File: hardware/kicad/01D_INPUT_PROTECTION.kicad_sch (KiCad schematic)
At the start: 0 parts

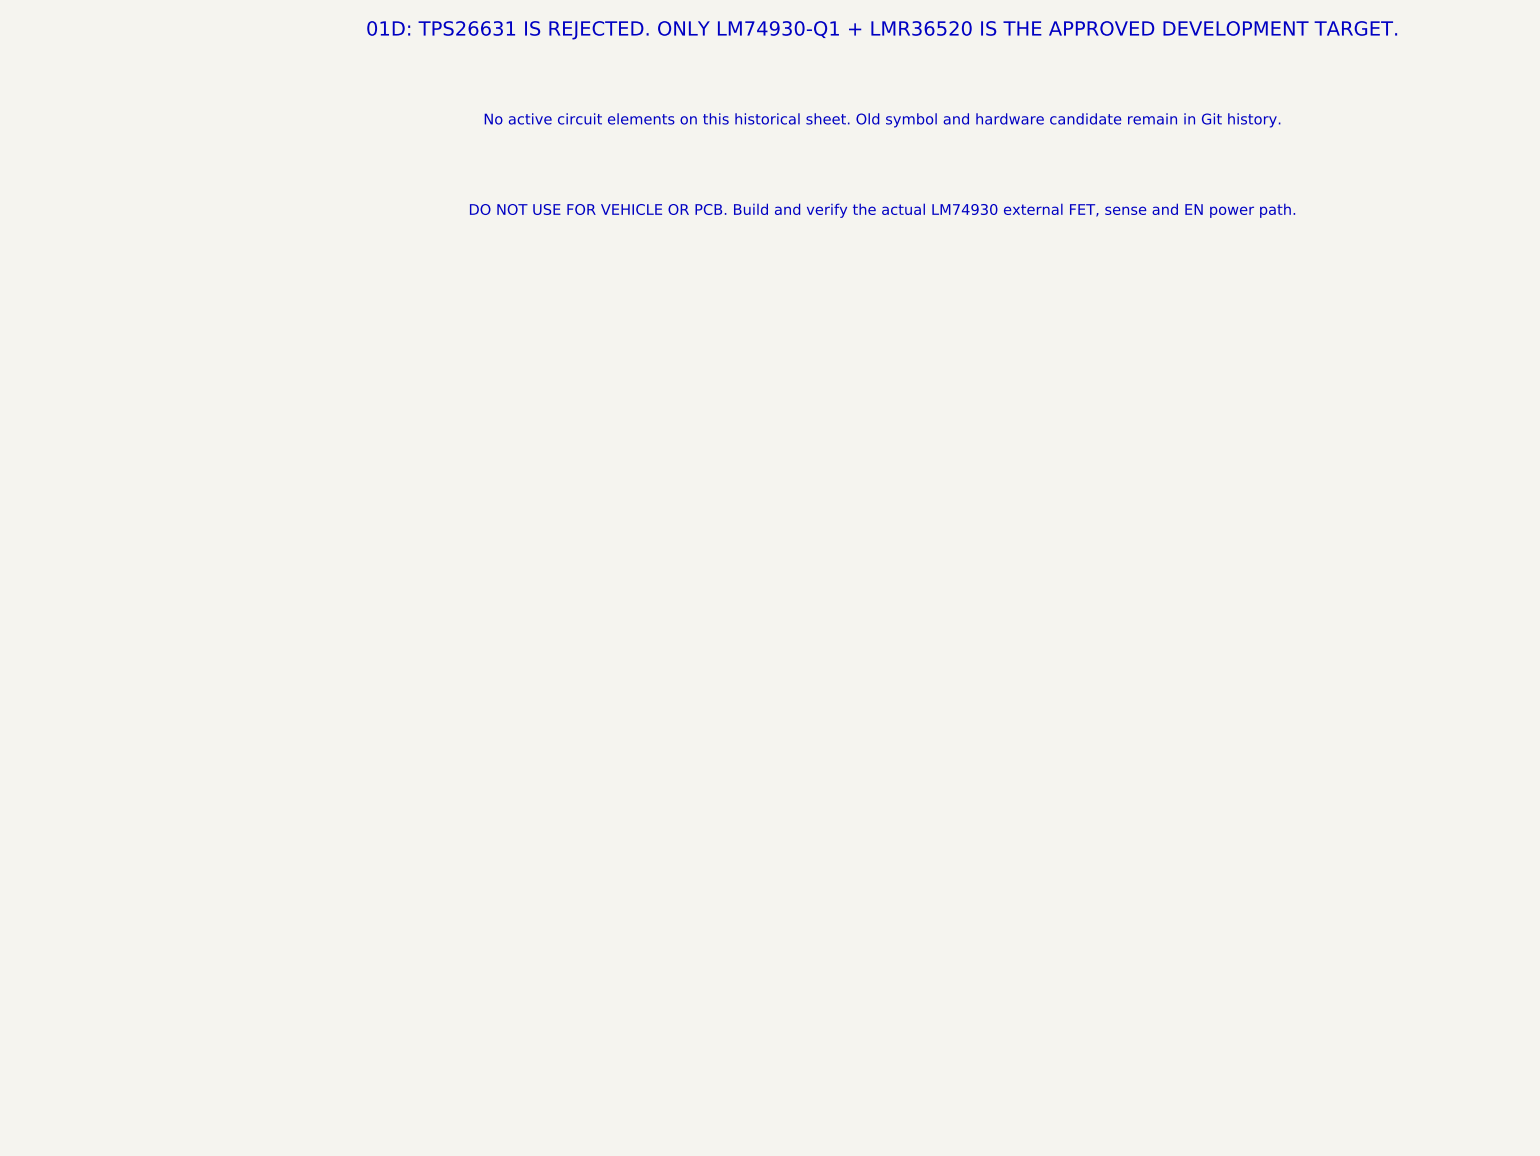
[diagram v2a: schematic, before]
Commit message: hardware(kicad): place LM74930-Q1 controller and datasheet-required 100nF capacitors in active 01D
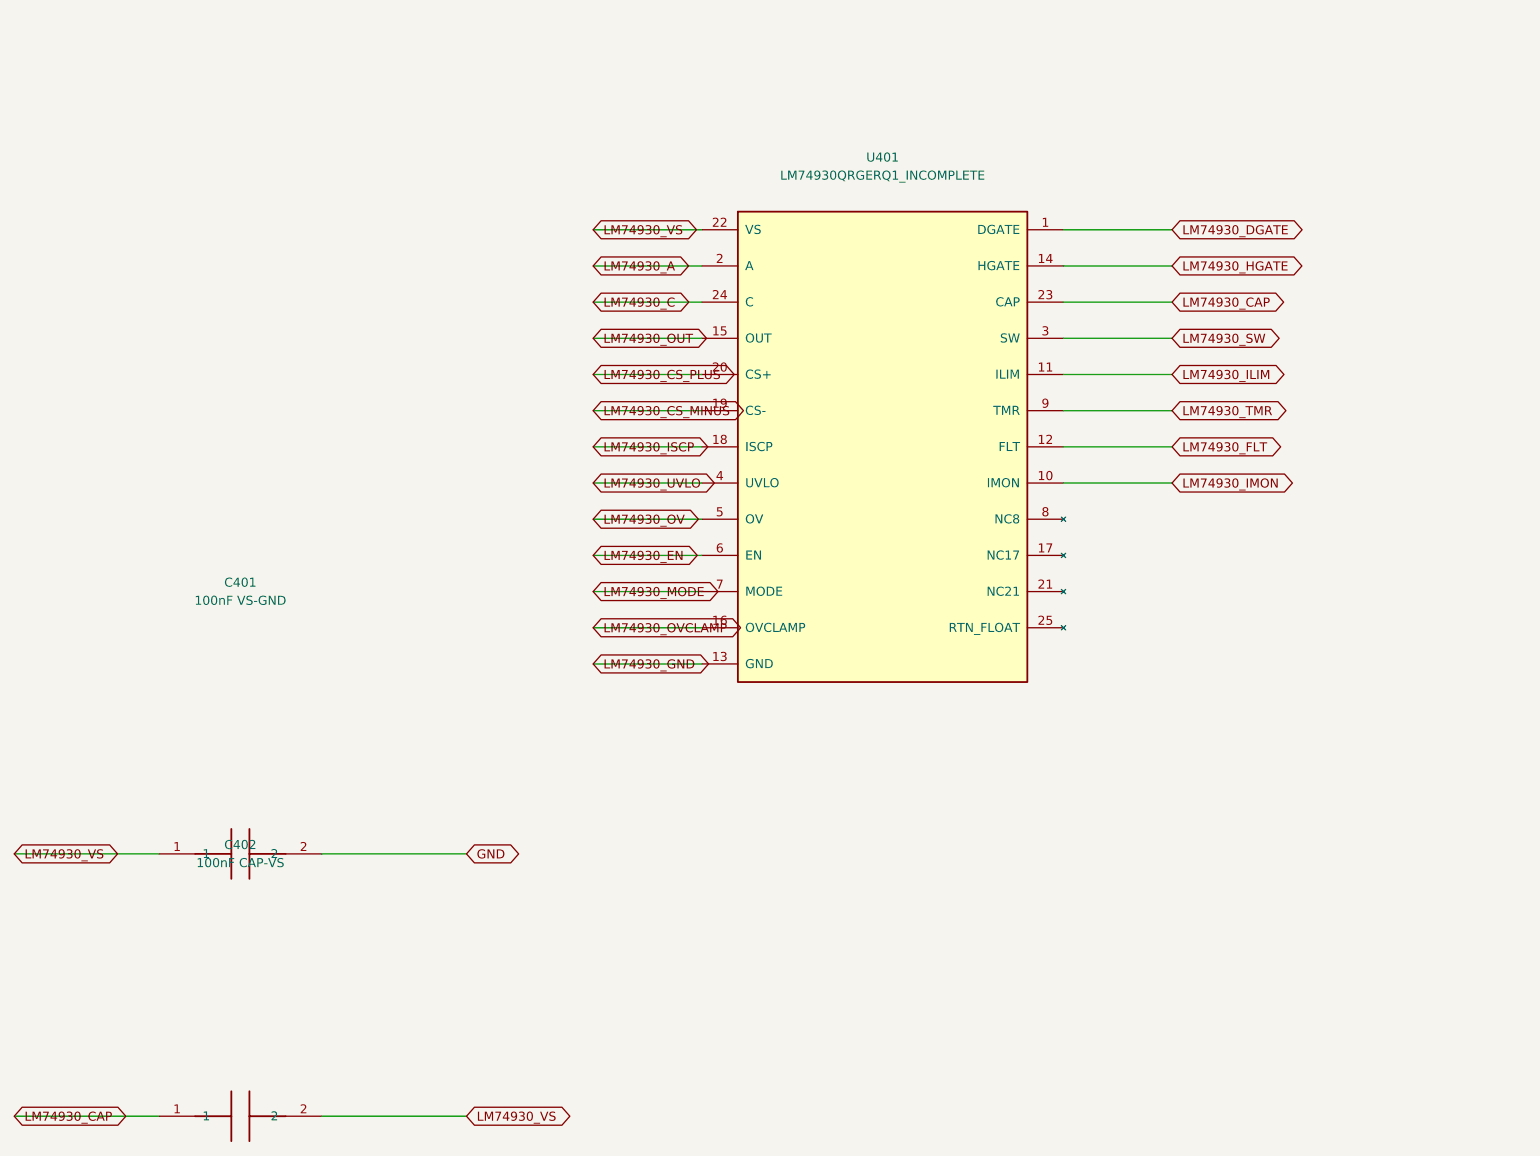
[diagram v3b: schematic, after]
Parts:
- added C401: 100nF VS-GND, Tripmaster:C_1206_3216, symbol Tripmaster_Sym:C
- added C402: 100nF CAP-VS, Tripmaster:C_1206_3216, symbol Tripmaster_Sym:C
- added U401: LM74930QRGERQ1_INCOMPLETE, Tripmaster:TI_LM74930_RGE0024T_FLOAT_EP, symbol TripTracer_V1:LM74930_Q1_RGE
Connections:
- new net GND: C401.2
- new net LM74930_A: U401.2 (A)
- new net LM74930_C: U401.24 (C)
- new net LM74930_CAP: C402.1, U401.23 (CAP)
- new net LM74930_CS_MINUS: U401.19 (CS-)
- new net LM74930_CS_PLUS: U401.20 (CS+)
- new net LM74930_DGATE: U401.1 (DGATE)
- new net LM74930_EN: U401.6 (EN)
- new net LM74930_FLT: U401.12 (FLT)
- new net LM74930_GND: U401.13 (GND)
- new net LM74930_HGATE: U401.14 (HGATE)
- new net LM74930_ILIM: U401.11 (ILIM)
- new net LM74930_IMON: U401.10 (IMON)
- new net LM74930_ISCP: U401.18 (ISCP)
- new net LM74930_MODE: U401.7 (MODE)
- new net LM74930_OUT: U401.15 (OUT)
- new net LM74930_OV: U401.5 (OV)
- new net LM74930_OVCLAMP: U401.16 (OVCLAMP)
- new net LM74930_SW: U401.3 (SW)
- new net LM74930_TMR: U401.9 (TMR)
- new net LM74930_UVLO: U401.4 (UVLO)
- new net LM74930_VS: C401.1, C402.2, U401.22 (VS)
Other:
- note removed: "01D: TPS26631 IS REJECTED. ONLY LM74930-Q1 + LMR36520 IS THE APPROVED DEVELOPMENT TARGET."
- note removed: "DO NOT USE FOR VEHICLE OR PCB. Build and verify the actual LM74930 external FET, sense and EN power path."
- note removed: "No active circuit elements on this historical sheet. Old symbol and hardware candidate remain in Git history."
- title: TripTracer V1 - 01D retired TPS26631 candidate -> TripTracer V1 - 01D LM74930-Q1 controller integration
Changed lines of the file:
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@@
-(kicad_sch (version 20250114) (generator "eeschema")
- (paper "A3")
- (title_block (title "TripTracer V1 - 01D retired TPS26631 candidate") (date "2026-10-14") (rev "RETired / LM74930-Q1 ONLY / NOT WIRED"))
- (text "01D: TPS26631 IS REJECTED. ONLY LM74930-Q1 + LMR36520 IS THE APPROVED DEVELOPMENT TARGET." (at 190.5 76.2 0) (effects (font (size 2 2))))
- (text "No active circuit elements on this historical sheet. Old symbol and hardware candidate remain in Git history." (at 190.5 88.9 0) (effects (font (size 1.5 1.5))))
- (text "DO NOT USE FOR VEHICLE OR PCB. Build and verify the actual LM74930 external FET, sense and EN power path." (at 190.5 101.6 0) (effects (font (size 1.5 1.5))))
- (sheet_instances (path "/a26d9b0c-7f10-4e5a-a65f-000000000064/a26d9b0c-7f10-4e5a-a65f-000000000065" (page "2.4")))
- (embedded_fonts no)
-)

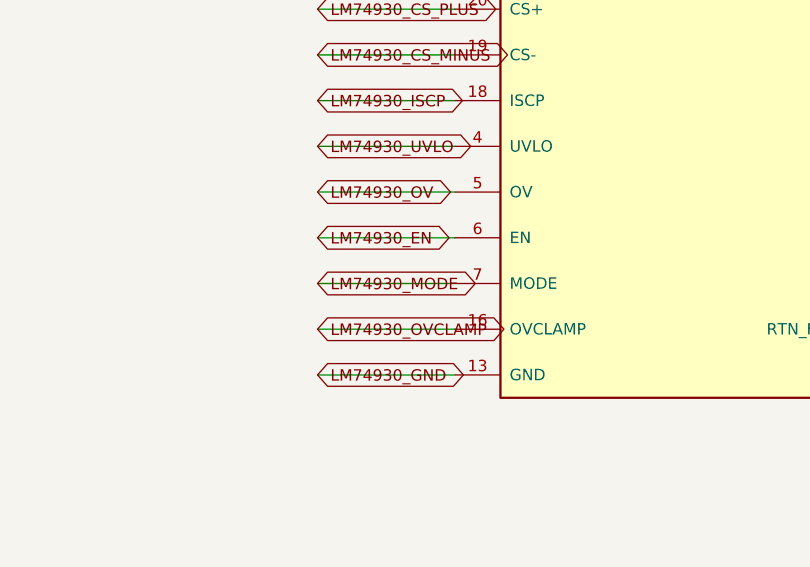
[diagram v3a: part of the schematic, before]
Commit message: hardware(power): tie LM74930 MODE high to VS to preserve reverse-current blocking
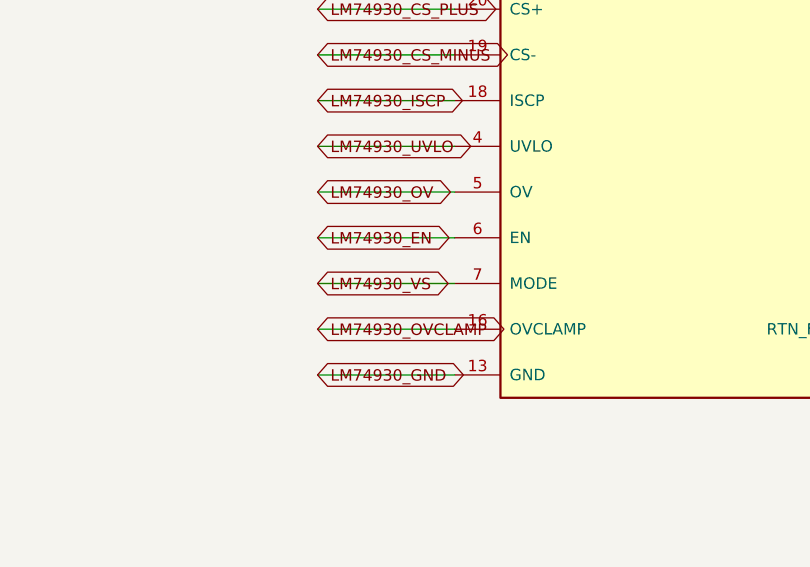
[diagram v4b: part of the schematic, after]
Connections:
- net LM74930_MODE is gone; now on net LM74930_VS: U401.7 (MODE)

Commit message: hardware(power): correct LM74930 VS capacitor to 1uF min nominal 1210 per load-dump design guidance
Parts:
- C401: value 100nF VS-GND -> 1uF >=100V VS-GND (Ceff verify); footprint Tripmaster:C_1206_3216 -> Tripmaster:C_1210_3225

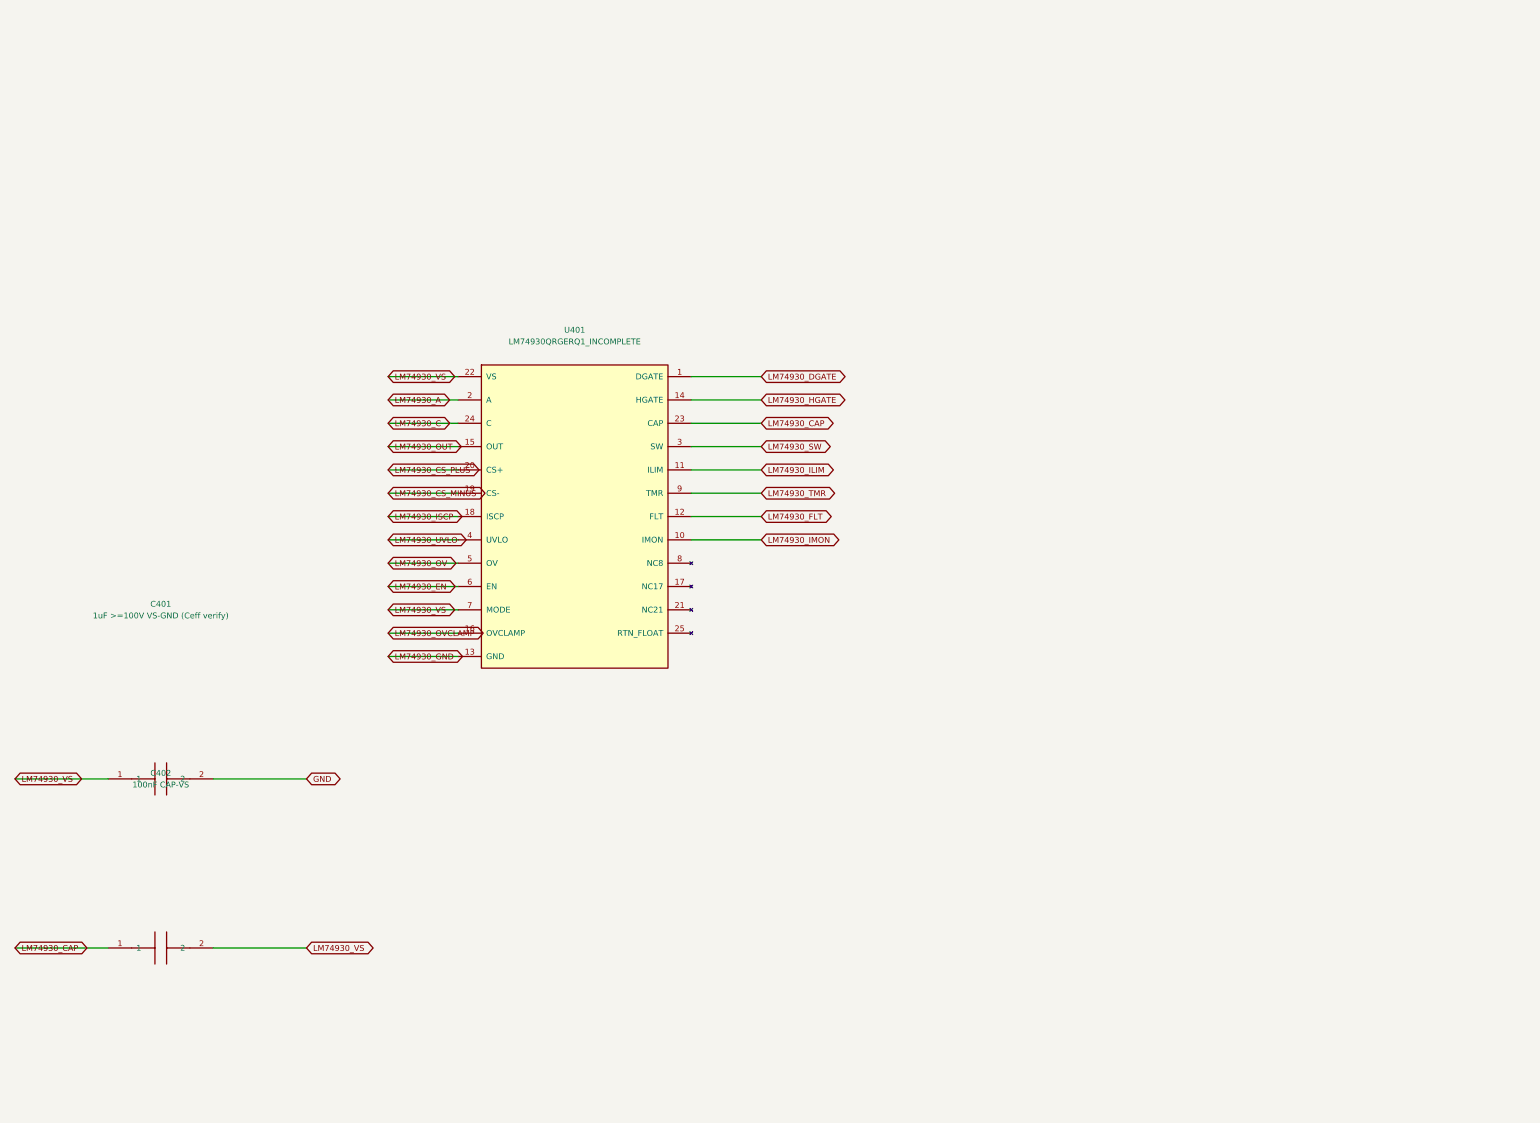
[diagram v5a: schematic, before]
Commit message: hardware(power): wire provisional back-to-back 100V FETs and 5mR Kelvin-shunt topology to LM74930
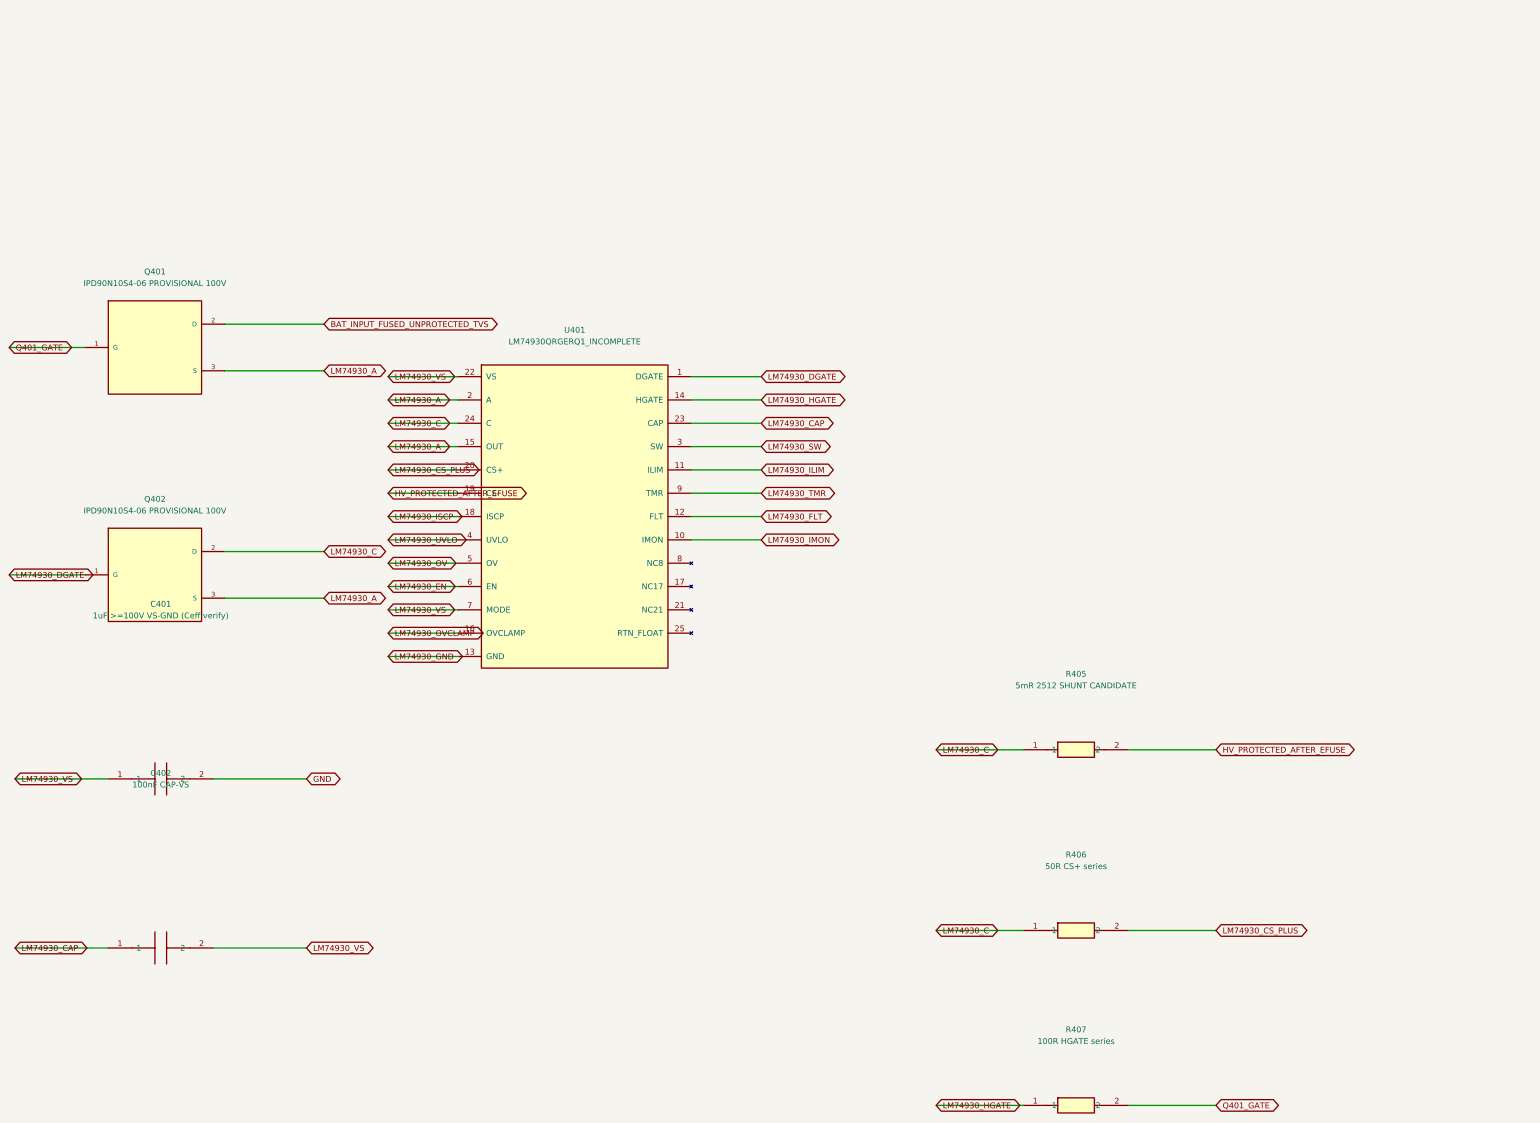
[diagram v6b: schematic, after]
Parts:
- added Q401, Q402: IPD90N10S4-06 PROVISIONAL 100V, Package_TO_SOT_SMD:TO-252-3_TabPin2, symbol TripTracer_V1:IPD90N10S4_06
- added R405: 5mR 2512 SHUNT CANDIDATE, Resistor_SMD:R_2512_6332Metric, symbol Tripmaster_Sym:R
- added R406: 50R CS+ series, Tripmaster:R_1206_3216, symbol Tripmaster_Sym:R
- added R407: 100R HGATE series, Tripmaster:R_1206_3216, symbol Tripmaster_Sym:R
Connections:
- net LM74930_OUT is gone; now on net LM74930_A: U401.15 (OUT)
- net LM74930_A: now also Q401.3 (S), Q402.3 (S)
- net LM74930_C: now also Q402.2 (D), R405.1, R406.1
- net LM74930_CS_PLUS: now also R406.2
- net LM74930_DGATE: now also Q402.1 (G)
- net LM74930_HGATE: now also R407.1
- net LM74930_CS_MINUS renamed HV_PROTECTED_AFTER_EFUSE
- net HV_PROTECTED_AFTER_EFUSE: now also R405.2
- new net BAT_INPUT_FUSED_UNPROTECTED_TVS: Q401.2 (D)
- new net Q401_GATE: Q401.1 (G), R407.2

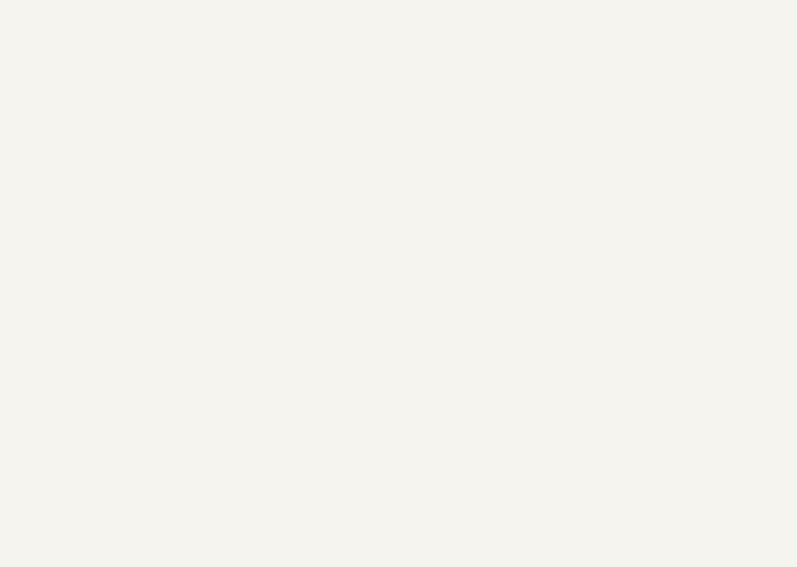
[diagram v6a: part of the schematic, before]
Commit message: hardware(power): add 100k physical EN pull-down for fail-off default
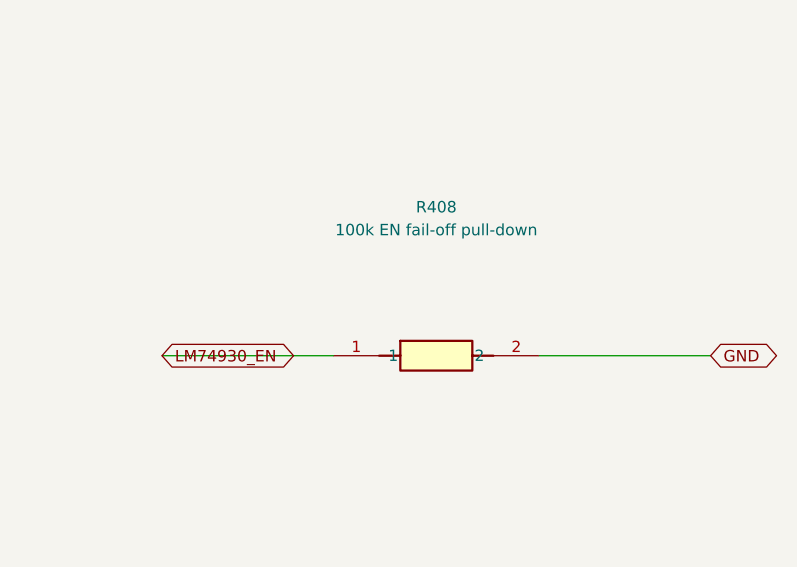
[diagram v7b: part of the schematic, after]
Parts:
- added R408: 100k EN fail-off pull-down, Tripmaster:R_1206_3216, symbol Tripmaster_Sym:R
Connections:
- net GND: now also R408.2
- net LM74930_EN: now also R408.1
